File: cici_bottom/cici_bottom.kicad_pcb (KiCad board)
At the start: 2 copper layers, 88.4 x 132.8 mm, 0 parts

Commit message: realizzato bottom e sistemato fori per viti
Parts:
- added REF**: MountingHole_2.2mm_M2_Pad, MountingHole:MountingHole_2.2mm_M2_Pad, F.Cu at (54.1, 30.1)
- added REF**: MountingHole_2.2mm_M2_Pad, MountingHole:MountingHole_2.2mm_M2_Pad, F.Cu at (94.2, 146.0)
- added REF**: MountingHole_2.2mm_M2_Pad, MountingHole:MountingHole_2.2mm_M2_Pad, F.Cu at (67.4, 135.0)
- added REF**: MountingHole_2.2mm_M2_Pad, MountingHole:MountingHole_2.2mm_M2_Pad, F.Cu at (120.8, 135.0)
- added REF**: MountingHole_2.2mm_M2_Pad, MountingHole:MountingHole_2.2mm_M2_Pad, F.Cu at (113.1, 70.8)
- added REF**: MountingHole_2.2mm_M2_Pad, MountingHole:MountingHole_2.2mm_M2_Pad, F.Cu at (94.1, 89.9)
- added REF**: MountingHole_2.2mm_M2_Pad, MountingHole:MountingHole_2.2mm_M2_Pad, F.Cu at (134.2, 30.1)
- added REF**: MountingHole_2.2mm_M2_Pad, MountingHole:MountingHole_2.2mm_M2_Pad, F.Cu at (75.0, 70.8)
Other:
- outline, holes or cut-outs redrawn
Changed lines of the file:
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@@
   (general
     (thickness 1.6)
-    (drawings 26)
+    (drawings 27)
     (tracks 0)
     (zones 0)
-    (modules 0)
+    (modules 8)
     (nets 1)
   )
@@
     (uvia_drill 0.1)
   )
+  (module MountingHole:MountingHole_2.2mm_M2_Pad (layer F.Cu)
+    (at 54.06 30.05)
+    (descr "Mounting Hole 2.2mm, M2")
+    (tags "mounting hole 2.2mm m2")
+    (attr virtual)
+    (fp_text reference REF** (at 0 -3.2) (layer Cmts.User) hide
+      (effects (font (size 1 1) (thickness 0.15)))
+    )
+    (fp_text value MountingHole_2.2mm_M2_Pad (at 0 3.2) (layer F.Fab) hide
+      (effects (font (size 1 1) (thickness 0.15)))
+    )
+    (fp_text user %R (at 0.3 0) (layer F.Fab) hide
+      (effects (font (size 1 1) (thickness 0.15)))
+    )
+    (fp_circle (center 0 0) (end 2.2 0) (layer Cmts.User) (width 0.15))
+    (fp_circle (center 0 0) (end 2.45 0) (layer F.CrtYd) (width 0.05))
+    (pad 1 thru_hole circle (at 0 0) (size 4.4 4.4) (drill 2.2) (layers *.Cu *.Mask))
+  )
+  (module MountingHole:MountingHole_2.2mm_M2_Pad (layer F.Cu)
+    (at 94.21 145.97)
+    (descr "Mounting Hole 2.2mm, M2")
+    (tags "mounting hole 2.2mm m2")
+    (attr virtual)
+    (fp_text reference REF** (at 0 -3.2) (layer Cmts.User) hide
+      (effects (font (size 1 1) (thickness 0.15)))
+    )
+    (fp_text value MountingHole_2.2mm_M2_Pad (at 0 3.2) (layer F.Fab) hide
+      (effects (font (size 1 1) (thickness 0.15)))
+    )
+    (fp_circle (center 0 0) (end 2.45 0) (layer F.CrtYd) (width 0.05))
+    (fp_circle (center 0 0) (end 2.2 0) (layer Cmts.User) (width 0.15))
+    (fp_text user %R (at 0.3 0) (layer F.Fab) hide
+      (effects (font (size 1 1) (thickness 0.15)))
+    )
+    (pad 1 thru_hole circle (at 0 0) (size 4.4 4.4) (drill 2.2) (layers *.Cu *.Mask))
+  )
+  (module MountingHole:MountingHole_2.2mm_M2_Pad (layer F.Cu)
+    (at 67.41 135)
+    (descr "Mounting Hole 2.2mm, M2")
+    (tags "mounting hole 2.2mm m2")
+    (attr virtual)
+    (fp_text reference REF** (at 0 -3.2) (layer Cmts.User) hide
+      (effects (font (size 1 1) (thickness 0.15)))
+    )
+    (fp_text value MountingHole_2.2mm_M2_Pad (at 0 3.2) (layer F.Fab) hide
+      (effects (font (size 1 1) (thickness 0.15)))
+    )
+    (fp_text user %R (at 0.3 0) (layer F.Fab) hide
+      (effects (font (size 1 1) (thickness 0.15)))
+    )
+    (fp_circle (center 0 0) (end 2.2 0) (layer Cmts.User) (width 0.15))
+    (fp_circle (center 0 0) (end 2.45 0) (layer F.CrtYd) (width 0.05))
+    (pad 1 thru_hole circle (at 0 0) (size 4.4 4.4) (drill 2.2) (layers *.Cu *.Mask))
+  )
+  (module MountingHole:MountingHole_2.2mm_M2_Pad (layer F.Cu)
+    (at 120.84 135)
+    (descr "Mounting Hole 2.2mm, M2")
+    (tags "mounting hole 2.2mm m2")
+    (attr virtual)
+    (fp_text reference REF** (at 0 -3.2) (layer Cmts.User) hide
+      (effects (font (size 1 1) (thickness 0.15)))
+    )
+    (fp_text value MountingHole_2.2mm_M2_Pad (at 0 3.2) (layer F.Fab) hide
+      (effects (font (size 1 1) (thickness 0.15)))
+    )
+    (fp_circle (center 0 0) (end 2.45 0) (layer F.CrtYd) (width 0.05))
+    (fp_circle (center 0 0) (end 2.2 0) (layer Cmts.User) (width 0.15))
+    (fp_text user %R (at 0.3 0) (layer F.Fab) hide
+      (effects (font (size 1 1) (thickness 0.15)))
+    )
+    (pad 1 thru_hole circle (at 0 0) (size 4.4 4.4) (drill 2.2) (layers *.Cu *.Mask))
+  )
+  (module MountingHole:MountingHole_2.2mm_M2_Pad (layer F.Cu)
+    (at 113.08 70.81)
+    (descr "Mounting Hole 2.2mm, M2")
+    (tags "mounting hole 2.2mm m2")
+    (attr virtual)
+    (fp_text reference REF** (at 0 -3.2) (layer Cmts.User) hide
+      (effects (font (size 1 1) (thickness 0.15)))
+    )
+    (fp_text value MountingHole_2.2mm_M2_Pad (at 0 3.2) (layer F.Fab) hide
+      (effects (font (size 1 1) (thickness 0.15)))
+    )
+    (fp_text user %R (at 0.3 0) (layer F.Fab) hide
+      (effects (font (size 1 1) (thickness 0.15)))
+    )
+    (fp_circle (center 0 0) (end 2.2 0) (layer Cmts.User) (width 0.15))
+    (fp_circle (center 0 0) (end 2.45 0) (layer F.CrtYd) (width 0.05))
+    (pad 1 thru_hole circle (at 0 0) (size 4.4 4.4) (drill 2.2) (layers *.Cu *.Mask))
+  )
+  (module MountingHole:MountingHole_2.2mm_M2_Pad (layer F.Cu)
+    (at 94.13 89.89)
+    (descr "Mounting Hole 2.2mm, M2")
+    (tags "mounting hole 2.2mm m2")
+    (attr virtual)
+    (fp_text reference REF** (at 0 -3.2) (layer Cmts.User) hide
+      (effects (font (size 1 1) (thickness 0.15)))
+    )
+    (fp_text value MountingHole_2.2mm_M2_Pad (at 0 3.2) (layer F.Fab) hide
+      (effects (font (size 1 1) (thickness 0.15)))
+    )
+    (fp_circle (center 0 0) (end 2.45 0) (layer F.CrtYd) (width 0.05))
+    (fp_circle (center 0 0) (end 2.2 0) (layer Cmts.User) (width 0.15))
+    (fp_text user %R (at 0.3 0) (layer F.Fab) hide
+      (effects (font (size 1 1) (thickness 0.15)))
+    )
+    (pad 1 thru_hole circle (at 0 0) (size 4.4 4.4) (drill 2.2) (layers *.Cu *.Mask))
+  )
+  (module MountingHole:MountingHole_2.2mm_M2_Pad (layer F.Cu)
+    (at 134.24 30.05)
+    (descr "Mounting Hole 2.2mm, M2")
+    (tags "mounting hole 2.2mm m2")
+    (attr virtual)
+    (fp_text reference REF** (at 0 -3.2) (layer Cmts.User) hide
+      (effects (font (size 1 1) (thickness 0.15)))
+    )
+    (fp_text value MountingHole_2.2mm_M2_Pad (at 0 3.2) (layer F.Fab) hide
+      (effects (font (size 1 1) (thickness 0.15)))
+    )
+    (fp_text user %R (at 0.3 0) (layer F.Fab) hide
+      (effects (font (size 1 1) (thickness 0.15)))
+    )
+    (fp_circle (center 0 0) (end 2.2 0) (layer Cmts.User) (width 0.15))
+    (fp_circle (center 0 0) (end 2.45 0) (layer F.CrtYd) (width 0.05))
+    (pad 1 thru_hole circle (at 0 0) (size 4.4 4.4) (drill 2.2) (layers *.Cu *.Mask))
+  )
+  (module MountingHole:MountingHole_2.2mm_M2_Pad (layer F.Cu)
+    (at 75.04 70.8)
+    (descr "Mounting Hole 2.2mm, M2")
+    (tags "mounting hole 2.2mm m2")
+    (attr virtual)
+    (fp_text reference REF** (at 0 -3.2) (layer Cmts.User) hide
+      (effects (font (size 1 1) (thickness 0.15)))
+    )
+    (fp_text value MountingHole_2.2mm_M2_Pad (at 0 3.2) (layer F.Fab) hide
+      (effects (font (size 1 1) (thickness 0.15)))
+    )
+    (fp_circle (center 0 0) (end 2.45 0) (layer F.CrtYd) (width 0.05))
+    (fp_circle (center 0 0) (end 2.2 0) (layer Cmts.User) (width 0.15))
+    (fp_text user %R (at 0.3 0) (layer F.Fab) hide
+      (effects (font (size 1 1) (thickness 0.15)))
+    )
+    (pad 1 thru_hole circle (at 0 0) (size 4.4 4.4) (drill 2.2) (layers *.Cu *.Mask))
+  )
+  (gr_line (start 58 27.2) (end 130.375 27.2) (layer F.SilkS) (width 0.5))
   (gr_arc (start 123.33 139.5) (end 124.246762 139.525368) (angle -115.3397962) (layer Edge.Cuts) (width 0.2))
   (gr_arc (start 100.95 153.61) (end 100.191271 152.951118) (angle -101.2542279) (layer Edge.Cuts) (width 0.2))
@@
   (gr_arc (start 92.925 116.1) (end 100.451863 154.482728) (angle -42.11246634) (layer Edge.Cuts) (width 0.2))
   (gr_arc (start 95.075 116.675) (end 63.61 139) (angle -43.7) (layer Edge.Cuts) (width 0.2))
-  (gr_arc (start 58.04 31.5) (end 58 33) (angle 176.9449491) (layer Edge.Cuts) (width 0.2))
-  (gr_arc (start 129.84 31.5) (end 130.375 33) (angle -140.7407538) (layer Edge.Cuts) (width 0.2))
-  (gr_line (start 58 33) (end 130.375 33) (layer Edge.Cuts) (width 0.2))
+  (gr_arc (start 58.04 31) (end 58 32) (angle 175.4) (layer Edge.Cuts) (width 0.2))
+  (gr_arc (start 129.84 31) (end 130.375 32) (angle -123.7064376) (layer Edge.Cuts) (width 0.2))
+  (gr_line (start 58 32) (end 130.375 32) (layer Edge.Cuts) (width 0.2))
   (gr_line (start 58 30) (end 130.375 30) (layer Edge.Cuts) (width 0.2))
   (gr_text CICI (at 94.125 153.125) (layer B.SilkS)

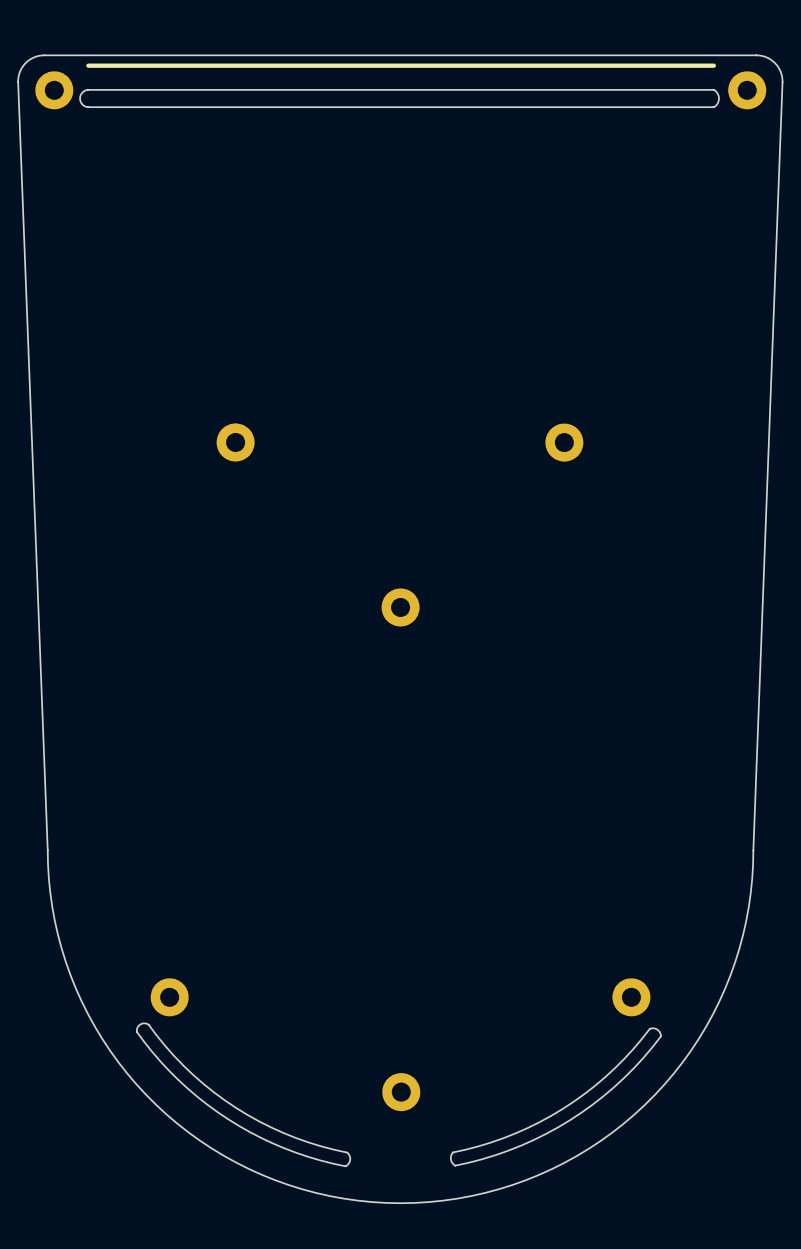
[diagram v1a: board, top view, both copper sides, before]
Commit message: creazione pezzo acrilico e sistemazione fori
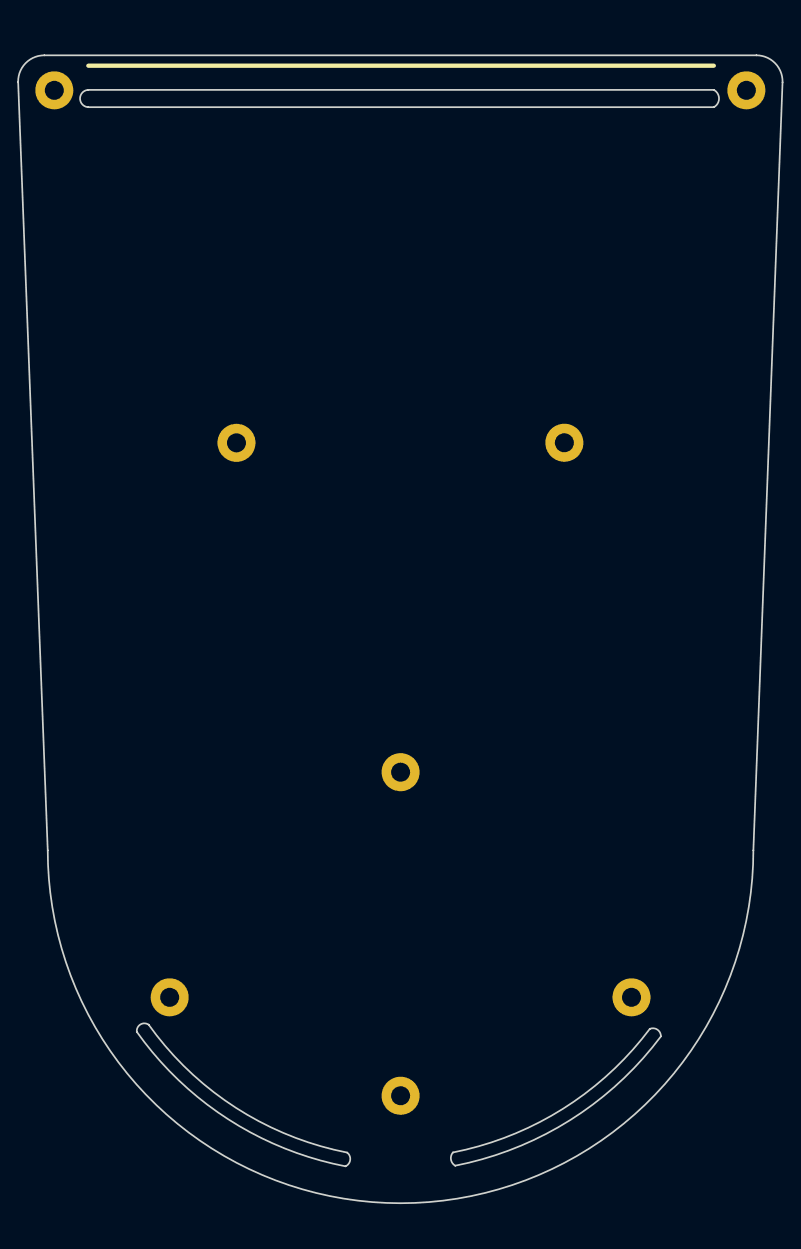
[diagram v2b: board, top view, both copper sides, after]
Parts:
- moved REF** 19.1 mm to (94.1, 109.0)
- moved 94.17 0.43 mm to (94.1, 146.4)
- moved REF** 0.11 mm to (75.1, 70.8)
- moved REF** 0.10 mm to (134.1, 30.1)
- renumbered REF** to 94.17
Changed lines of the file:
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@@
   )
   (module MountingHole:MountingHole_2.2mm_M2_Pad (layer F.Cu)
-    (at 94.21 145.97)
+    (at 94.13 146.39)
     (descr "Mounting Hole 2.2mm, M2")
     (tags "mounting hole 2.2mm m2")
     (attr virtual)
-    (fp_text reference REF** (at 0 -3.2) (layer Cmts.User) hide
+    (fp_text reference 94.17 (at 0 -3.2) (layer Cmts.User) hide
       (effects (font (size 1 1) (thickness 0.15)))
     )
@@
   )
   (module MountingHole:MountingHole_2.2mm_M2_Pad (layer F.Cu)
-    (at 120.84 135)
+    (at 120.85 135)
     (descr "Mounting Hole 2.2mm, M2")
     (tags "mounting hole 2.2mm m2")
@@
   )
   (module MountingHole:MountingHole_2.2mm_M2_Pad (layer F.Cu)
-    (at 113.08 70.81)
+    (at 113.08 70.83)
     (descr "Mounting Hole 2.2mm, M2")
     (tags "mounting hole 2.2mm m2")
@@
   )
   (module MountingHole:MountingHole_2.2mm_M2_Pad (layer F.Cu)
-    (at 94.13 89.89)
+    (at 94.13 108.95)
     (descr "Mounting Hole 2.2mm, M2")
     (tags "mounting hole 2.2mm m2")
@@
   )
   (module MountingHole:MountingHole_2.2mm_M2_Pad (layer F.Cu)
-    (at 134.24 30.05)
+    (at 134.14 30.05)
     (descr "Mounting Hole 2.2mm, M2")
     (tags "mounting hole 2.2mm m2")
@@
   )
   (module MountingHole:MountingHole_2.2mm_M2_Pad (layer F.Cu)
-    (at 75.04 70.8)
+    (at 75.14 70.84)
     (descr "Mounting Hole 2.2mm, M2")
     (tags "mounting hole 2.2mm m2")
@@
   (gr_line (start 58 32) (end 130.375 32) (layer Edge.Cuts) (width 0.2))
   (gr_line (start 58 30) (end 130.375 30) (layer Edge.Cuts) (width 0.2))
-  (gr_text CICI (at 94.125 153.125) (layer B.SilkS)
+  (gr_text CICI (at 94.125 153.3) (layer B.SilkS)
     (effects (font (size 4 4) (thickness 0.5)) (justify mirror))
   )
-  (gr_text -zanni- (at 94.125 149.15) (layer B.SilkS)
+  (gr_text -zanni- (at 94.125 149.7) (layer B.SilkS)
     (effects (font (size 1.5 1.5) (thickness 0.3)) (justify mirror))
   )

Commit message: prima versione conclusa. inizio seconda
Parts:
- moved REF** 4.55 mm to (54.1, 25.5)
- moved REF** 4.55 mm to (134.1, 25.5)
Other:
- board size 88.4 x 132.8 mm -> 88.4 x 140.3 mm
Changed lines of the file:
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@@
   )
   (module MountingHole:MountingHole_2.2mm_M2_Pad (layer F.Cu)
-    (at 54.06 30.05)
+    (at 54.06 25.5)
     (descr "Mounting Hole 2.2mm, M2")
     (tags "mounting hole 2.2mm m2")
@@
   )
   (module MountingHole:MountingHole_2.2mm_M2_Pad (layer F.Cu)
-    (at 134.14 30.05)
+    (at 134.14 25.5)
     (descr "Mounting Hole 2.2mm, M2")
     (tags "mounting hole 2.2mm m2")
@@
     (pad 1 thru_hole circle (at 0 0) (size 4.4 4.4) (drill 2.2) (layers *.Cu *.Mask))
   )
-  (gr_line (start 58 27.2) (end 130.375 27.2) (layer F.SilkS) (width 0.5))
-  (gr_arc (start 123.33 139.5) (end 124.246762 139.525368) (angle -115.3397962) (layer Edge.Cuts) (width 0.2))
-  (gr_arc (start 100.95 153.61) (end 100.191271 152.951118) (angle -101.2542279) (layer Edge.Cuts) (width 0.2))
-  (gr_arc (start 64.48 138.89) (end 64.98 138.17) (angle -131.9838884) (layer Edge.Cuts) (width 0.2))
-  (gr_arc (start 87.37 153.7) (end 87.750789 154.553857) (angle -117.7344543) (layer Edge.Cuts) (width 0.2))
-  (gr_arc (start 92.926271 116.091118) (end 100.191271 152.951118) (angle -41.92680981) (layer Edge.Cuts) (width 0.2))
-  (gr_arc (start 95.075 116.675) (end 64.98 138.17) (angle -43.3547479) (layer Edge.Cuts) (width 0.2))
-  (gr_arc (start 92.925 116.1) (end 100.451863 154.482728) (angle -42.11246634) (layer Edge.Cuts) (width 0.2))
-  (gr_arc (start 95.075 116.675) (end 63.61 139) (angle -43.7) (layer Edge.Cuts) (width 0.2))
-  (gr_arc (start 58.04 31) (end 58 32) (angle 175.4) (layer Edge.Cuts) (width 0.2))
-  (gr_arc (start 129.84 31) (end 130.375 32) (angle -123.7064376) (layer Edge.Cuts) (width 0.2))
-  (gr_line (start 58 32) (end 130.375 32) (layer Edge.Cuts) (width 0.2))
-  (gr_line (start 58 30) (end 130.375 30) (layer Edge.Cuts) (width 0.2))
-  (gr_text CICI (at 94.125 153.3) (layer B.SilkS)
-    (effects (font (size 4 4) (thickness 0.5)) (justify mirror))
+  (gr_arc (start 85.92 155.28) (end 86.300789 156.133857) (angle -117.7344543) (layer Edge.Cuts) (width 0.2))
+  (gr_arc (start 63.03 140.47) (end 63.53 139.75) (angle -131.9838884) (layer Edge.Cuts) (width 0.2))
+  (gr_arc (start 93.625 118.255) (end 63.53 139.75) (angle -43.3547479) (layer Edge.Cuts) (width 0.2))
+  (gr_arc (start 93.625 118.255) (end 62.16 140.58) (angle -43.7) (layer Edge.Cuts) (width 0.2))
+  (gr_line (start 58 22.9) (end 130.375 22.9) (layer F.SilkS) (width 0.5))
+  (gr_arc (start 125.32217 140.491405) (end 126.238932 140.516773) (angle -115.3397962) (layer Edge.Cuts) (width 0.2))
+  (gr_arc (start 102.478137 154.977272) (end 101.719408 154.31839) (angle -101.2542279) (layer Edge.Cuts) (width 0.2))
+  (gr_arc (start 94.666271 117.411118) (end 101.719408 154.31839) (angle -42.88924805) (layer Edge.Cuts) (width 0.2))
+  (gr_arc (start 94.665 117.42) (end 101.98 155.85) (angle -43.03690352) (layer Edge.Cuts) (width 0.2))
+  (gr_arc (start 58.16 25.68) (end 58.12 26.68) (angle 175.4) (layer Edge.Cuts) (width 0.2))
+  (gr_arc (start 129.96 25.68) (end 130.495 26.68) (angle -123.7064376) (layer Edge.Cuts) (width 0.2))
+  (gr_line (start 58.12 26.68) (end 130.495 26.68) (layer Edge.Cuts) (width 0.2))
+  (gr_line (start 58.12 24.68) (end 130.495 24.68) (layer Edge.Cuts) (width 0.2))
+  (gr_text CICI (at 94.13 155.5) (layer B.SilkS)
+    (effects (font (size 3 4) (thickness 0.5)) (justify mirror))
   )
-  (gr_text -zanni- (at 94.125 149.7) (layer B.SilkS)
+  (gr_text -zanni- (at 94.13 152) (layer B.SilkS)
     (effects (font (size 1.5 1.5) (thickness 0.3)) (justify mirror))
   )
-  (gr_arc (start 92.925 116.1) (end 100.3 155.55) (angle -43.4) (layer B.SilkS) (width 0.5))
-  (gr_arc (start 95.075 116.675) (end 62.9 139.75) (angle -44.1) (layer B.SilkS) (width 0.5))
-  (gr_arc (start 94.15 117.85) (end 54.525 118.4) (angle -179.2) (layer B.SilkS) (width 0.5))
-  (gr_line (start 54.525 118.4) (end 51.100929 34) (layer B.SilkS) (width 0.5))
-  (gr_line (start 137.153817 34) (end 133.778817 117.853305) (layer B.SilkS) (width 0.5))
-  (gr_line (start 58 27.2) (end 130.375 27.2) (layer B.SilkS) (width 0.5))
-  (gr_arc (start 135.3 29.025) (end 138.325 29.125) (angle -91.9) (layer Edge.Cuts) (width 0.2))
-  (gr_line (start 138.325 29.125) (end 134.95 118) (layer Edge.Cuts) (width 0.2))
-  (gr_arc (start 94.125 118) (end 53.3 118) (angle -180) (layer Edge.Cuts) (width 0.2))
-  (gr_line (start 53.3 118) (end 49.875929 29.099977) (layer Edge.Cuts) (width 0.2))
-  (gr_arc (start 52.9 29.025) (end 52.9 26) (angle -91.4) (layer Edge.Cuts) (width 0.2))
-  (gr_line (start 52.9 26) (end 135.3 26) (layer Edge.Cuts) (width 0.2))
+  (gr_arc (start 94.1227 117.42) (end 100.53 158.33) (angle -43.4) (layer B.SilkS) (width 0.5))
+  (gr_arc (start 94.1227 117.42) (end 61.73 143.22) (angle -42.90512361) (layer B.SilkS) (width 0.5))
+  (gr_arc (start 94.1227 117.42) (end 51.100929 118.4) (angle -179.2) (layer B.SilkS) (width 0.5))
+  (gr_line (start 51.100929 118.4) (end 51.100929 30) (layer B.SilkS) (width 0.5))
+  (gr_line (start 137.153817 30) (end 137.153382 117.859999) (layer B.SilkS) (width 0.5))
+  (gr_line (start 58 22.9) (end 130.375 22.9) (layer B.SilkS) (width 0.5))
+  (gr_arc (start 135.3 24.725) (end 138.325 24.825) (angle -91.9) (layer Edge.Cuts) (width 0.2))
+  (gr_line (start 138.325 24.825) (end 138.324097 117.58) (layer Edge.Cuts) (width 0.2))
+  (gr_arc (start 94.1 117.79) (end 49.875903 118) (angle -180) (layer Edge.Cuts) (width 0.2))
+  (gr_line (start 49.875903 118) (end 49.875903 24.798907) (layer Edge.Cuts) (width 0.2))
+  (gr_arc (start 52.9 24.725) (end 52.9 21.7) (angle -91.4) (layer Edge.Cuts) (width 0.2))
+  (gr_line (start 52.9 21.7) (end 135.299651 21.698348) (layer Edge.Cuts) (width 0.2))
 )
